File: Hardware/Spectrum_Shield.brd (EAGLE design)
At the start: 59.7 x 53.3 mm, 27 parts, among them U1 ARDUINO_R3_SHIELD, U2 MSGEQ7SOIC, U3 MSGEQ7SOIC

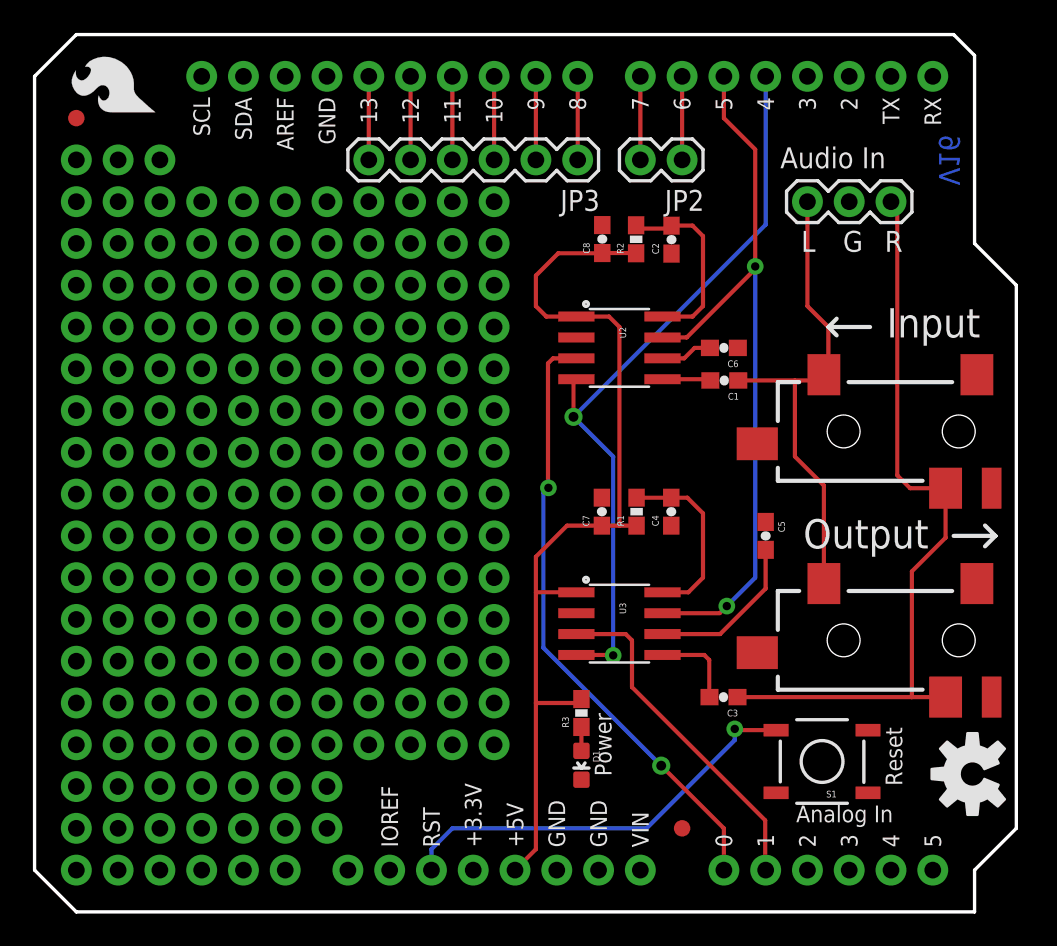
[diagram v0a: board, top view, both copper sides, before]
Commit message: Added stand offs, fixed silk.  QC list / attributes
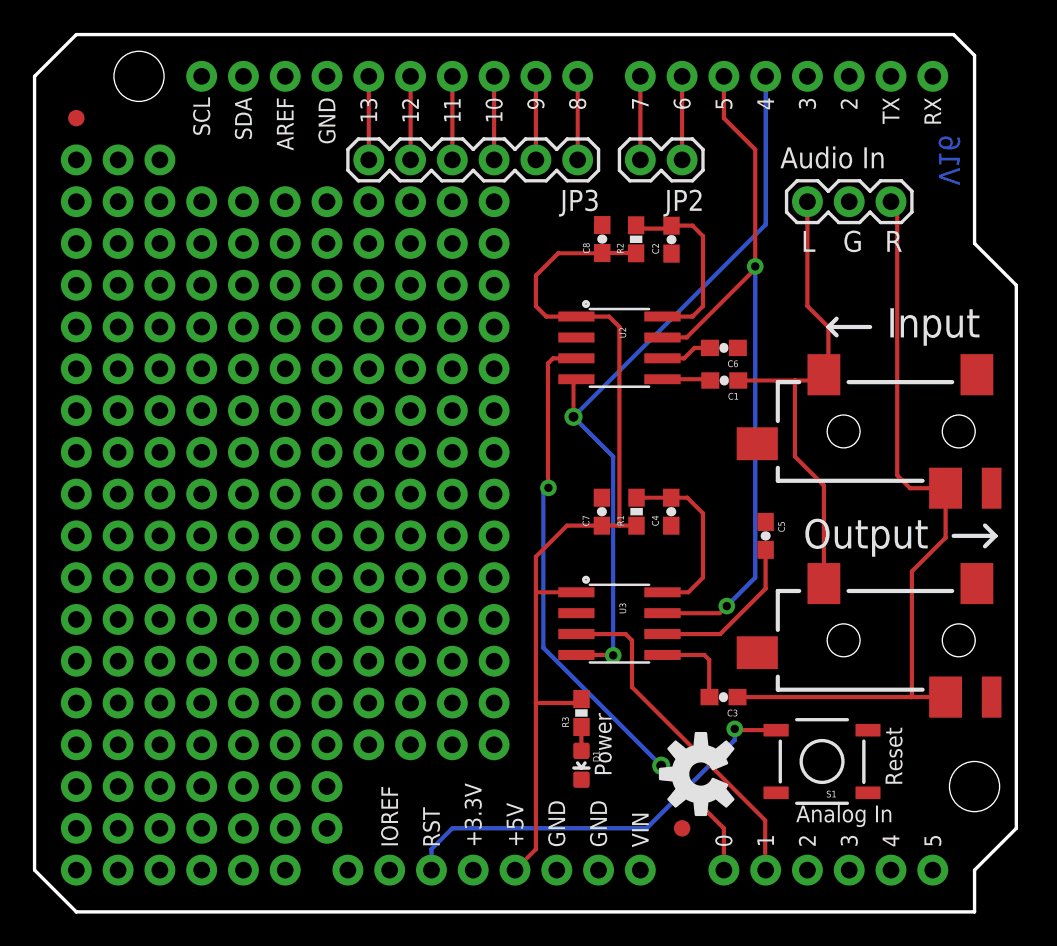
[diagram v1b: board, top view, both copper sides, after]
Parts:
- removed LOGO2: SFE_LOGO_FLAME.2_INCH, SparkFun-Aesthetics:SFE_LOGO_FLAME_.2
- added U$1, U$3: (no value), SparkFun-Electromechanical:STAND-OFF-TIGHT
- moved LOGO1 16.5 mm to (40.5, 8.38)
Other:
- board text added: "Chris Taylor"
- board text removed: "J. Lindblom"
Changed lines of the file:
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@@
 <?xml version="1.0" encoding="utf-8"?>
 <!DOCTYPE eagle SYSTEM "eagle.dtd">
-<eagle version="7.1.0">
+<eagle version="7.2.0">
 <drawing>
 <settings>
@@
 <wire x1="57.785" y1="23.495" x2="58.42" y2="22.86" width="0.254" layer="21"/>
 <wire x1="57.785" y1="22.225" x2="58.42" y2="22.86" width="0.254" layer="21"/>
-<text x="34.671" y="-15.367" size="1.778" layer="51" font="vector" ratio="12">J. Lindblom</text>
+<text x="39.751" y="-15.367" size="1.778" layer="51" font="vector" ratio="12">Chris Taylor</text>
 <text x="20.574" y="-17.907" size="1.778" layer="51" font="vector" ratio="12">Revised by: P. Alberts</text>
 <dimension x1="-20.32" y1="0" x2="-20.32" y2="53.34" x3="-19.05" y3="26.67" textsize="1.778" textratio="15" layer="47" unit="inch" visible="yes"/>
@@
 </element>
 <element name="FRAME1" library="SparkFun-Aesthetics" package="CREATIVE_COMMONS" value="FRAME-LETTER" x="8.89" y="-15.24"/>
-<element name="LOGO1" library="SparkFun-Aesthetics" package="OSHW-LOGO-M" value="OSHW-LOGOM" x="57.023" y="8.382" rot="R90"/>
-<element name="LOGO2" library="SparkFun-Aesthetics" package="SFE_LOGO_FLAME_.2" value="SFE_LOGO_FLAME.2_INCH" x="7.62" y="48.26" rot="R90"/>
+<element name="LOGO1" library="SparkFun-Aesthetics" package="OSHW-LOGO-M" value="OSHW-LOGOM" x="40.513" y="8.382" rot="R90"/>
 <element name="LOGO3" library="SparkFun-Aesthetics" package="SFE_LOGO_NAME_FLAME_.1" value="SFE_LOGO_NAME_FLAME.1_INCH" x="36.83" y="20.32" rot="MR90"/>
+<element name="U$1" library="SparkFun-Electromechanical" package="STAND-OFF-TIGHT" value="" x="57.15" y="7.62"/>
+<element name="U$3" library="SparkFun-Electromechanical" package="STAND-OFF-TIGHT" value="" x="6.35" y="50.8"/>
 </elements>
 <signals>

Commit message: Fixed QC Checklist Items
1) Currently there are two 4-way junctions: both below each MSGEQ7
symbol, each 4-way needs to split up into two 3-way junctions.

(2) On the R3 symbol the VCC net crosses over the RESET net. It would be
nice to reorganize these nets to eliminate the intersection all
together.

(3) The Audio jacks are currently named Audiojack1 and 2, these should
have a name that uses the proper connector prefix (JPx) x being a number

(4) Two vias have tStop and bStop polygons set over them: the first is
right next to the OSHW silk, and the other is below U2 (the upper MSGEQ7
IC). These are not used for testing

(5) Audio jacks need a name and value in BRD

(6) Need measures that include the standoffs

(7) As of now the name of the product is not on the board; the previous
rev was without a silk for the product name as well (figured I would
bring it up). Also, it would be nice to get an SFE flame on the top of
the board, like the previous rev.

that's it
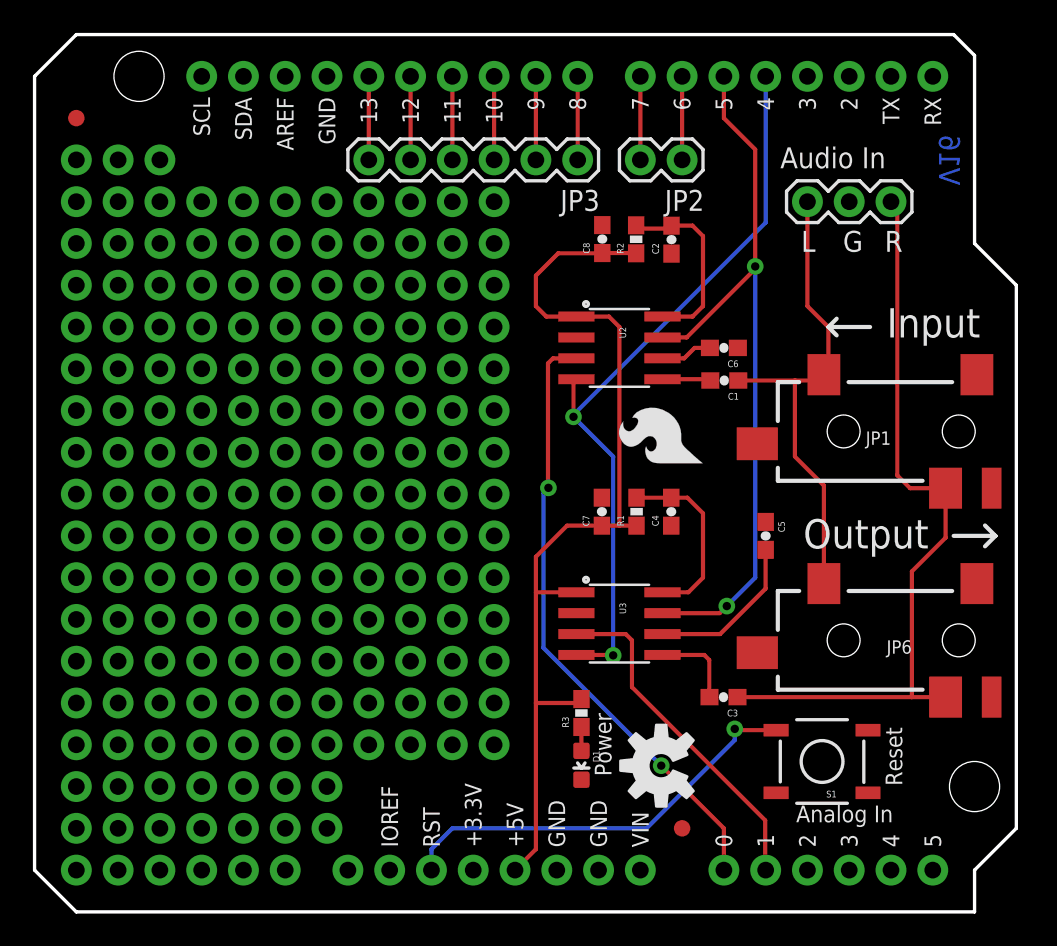
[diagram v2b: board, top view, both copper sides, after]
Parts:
- added LOGO2: SFE_LOGO_FLAME.2_INCH, SparkFun-Aesthetics:SFE_LOGO_FLAME_.2
- JP1, JP6: value (none) -> 3.5mm Audio Jack
- moved LOGO3 2.54 mm to (39.4, 20.3)
- moved LOGO1 2.47 mm to (38.1, 8.89)
- renumbered AUDIOJACK1 to JP1, AUDIOJACK2 to JP6
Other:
- board text added: "Center point to center point Stand Off distance"
- board text added: "Spectrum Shield"
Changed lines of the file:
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@@
 <?xml version="1.0" encoding="utf-8"?>
 <!DOCTYPE eagle SYSTEM "eagle.dtd">
-<eagle version="7.2.0">
+<eagle version="7.1.0">
 <drawing>
 <settings>
@@
 <layer number="47" name="Measures" color="7" fill="1" visible="no" active="yes"/>
 <layer number="48" name="Document" color="7" fill="1" visible="no" active="yes"/>
-<layer number="49" name="Reference" color="7" fill="1" visible="no" active="yes"/>
+<layer number="49" name="Reference" color="7" fill="1" visible="yes" active="yes"/>
 <layer number="50" name="dxf" color="7" fill="1" visible="no" active="yes"/>
 <layer number="51" name="tDocu" color="6" fill="1" visible="yes" active="yes"/>
@@
 <dimension x1="-20.32" y1="0" x2="-20.32" y2="53.34" x3="-19.05" y3="26.67" textsize="1.778" textratio="15" layer="47" unit="inch" visible="yes"/>
 <dimension x1="0" y1="59.69" x2="59.69" y2="59.69" x3="29.845" y3="58.42" textsize="1.778" textratio="15" layer="47" unit="inch" visible="yes"/>
+<dimension x1="6.35" y1="57.15" x2="57.15" y2="57.15" x3="31.75" y3="55.88" textsize="1.778" textratio="15" layer="47" unit="inch" visible="yes"/>
+<dimension x1="67.31" y1="7.62" x2="67.31" y2="50.8" x3="68.58" y3="29.21" textsize="1.778" textratio="15" layer="47" unit="inch" visible="yes"/>
+<text x="71.12" y="12.7" size="0.8128" layer="47" font="vector" ratio="15" rot="R90">Center point to center point Stand Off distance</text>
+<text x="46.99" y="55.88" size="0.8128" layer="47" font="vector" ratio="15" rot="R180">Center point to center point Stand Off distance</text>
+<text x="39.37" y="34.29" size="1.27" layer="22" font="vector" ratio="15" rot="MR270">Spectrum Shield</text>
 </plain>
 <attributes>
@@
 </autorouter>
 <elements>
-<element name="C1" library="SparkFun-Capacitors" package="0603-CAP" value="1nF" x="41.9354" y="32.3088" rot="R180">
+<element name="C1" library="SparkFun-Capacitors" package="0603-CAP" value="1nF" x="41.9354" y="32.3088" smashed="yes" rot="R180">
 <attribute name="PROD_ID" value="CAP-07886" x="41.9354" y="32.3088" size="1.778" layer="27" rot="R180" display="off"/>
 <attribute name="VALUE" value="1nF" x="41.9354" y="32.3088" size="1.778" layer="27" rot="R180" display="off"/>
+<attribute name="NAME" x="42.8244" y="31.5468" size="0.4064" layer="25" font="vector" rot="R180"/>
+<attribute name="VALUE" x="41.6814" y="31.5468" size="0.4064" layer="27" font="vector" rot="R180"/>
 </element>
 <element name="C2" library="SparkFun-Capacitors" package="0603-CAP" value="33pF" x="38.724840625" y="40.87368125" rot="R90">
@@
 <element name="JP4" library="SparkFun" package="FIDUCIAL-1X2" value="FIDUCIAL1X2" x="39.37" y="5.08"/>
 <element name="JP5" library="SparkFun" package="FIDUCIAL-1X2" value="FIDUCIAL1X2" x="2.54" y="48.26"/>
-<element name="AUDIOJACK1" library="SparkFun-Connectors" package="AUDIO-JACK-3.5MM-SMD" value="" x="59.69" y="29.21" rot="R180">
+<element name="JP1" library="SparkFun-Connectors" package="AUDIO-JACK-3.5MM-SMD" value="3.5mm Audio Jack" x="59.69" y="29.21" smashed="yes" rot="R180">
 <attribute name="PROD_ID" value="CONN-10353" x="59.69" y="29.21" size="1.778" layer="27" font="vector" ratio="15" rot="R180" display="off"/>
-</element>
-<element name="AUDIOJACK2" library="SparkFun-Connectors" package="AUDIO-JACK-3.5MM-SMD" value="" x="59.69" y="16.51" rot="R180">
+<attribute name="NAME" x="52.07" y="29.21" size="0.8128" layer="25" font="vector" rot="R180"/>
+<attribute name="VALUE" x="57.15" y="27.94" size="0.8128" layer="27" font="vector" rot="R180"/>
+</element>
+<element name="JP6" library="SparkFun-Connectors" package="AUDIO-JACK-3.5MM-SMD" value="3.5mm Audio Jack" x="59.69" y="16.51" smashed="yes" rot="R180">
 <attribute name="PROD_ID" value="CONN-10353" x="59.69" y="16.51" size="1.778" layer="27" font="vector" ratio="15" rot="R180" display="off"/>
+<attribute name="NAME" x="53.34" y="16.51" size="0.8128" layer="25" font="vector" rot="R180"/>
+<attribute name="VALUE" x="57.15" y="17.78" size="0.8128" layer="27" font="vector" rot="R180"/>
 </element>
 <element name="FRAME1" library="SparkFun-Aesthetics" package="CREATIVE_COMMONS" value="FRAME-LETTER" x="8.89" y="-15.24"/>
-<element name="LOGO1" library="SparkFun-Aesthetics" package="OSHW-LOGO-M" value="OSHW-LOGOM" x="40.513" y="8.382" rot="R90"/>
-<element name="LOGO3" library="SparkFun-Aesthetics" package="SFE_LOGO_NAME_FLAME_.1" value="SFE_LOGO_NAME_FLAME.1_INCH" x="36.83" y="20.32" rot="MR90"/>
+<element name="LOGO1" library="SparkFun-Aesthetics" package="OSHW-LOGO-M" value="OSHW-LOGOM" x="38.1" y="8.89" rot="R90"/>
+<element name="LOGO3" library="SparkFun-Aesthetics" package="SFE_LOGO_NAME_FLAME_.1" value="SFE_LOGO_NAME_FLAME.1_INCH" x="39.37" y="20.32" rot="MR90"/>
 <element name="U$1" library="SparkFun-Electromechanical" package="STAND-OFF-TIGHT" value="" x="57.15" y="7.62"/>
 <element name="U$3" library="SparkFun-Electromechanical" package="STAND-OFF-TIGHT" value="" x="6.35" y="50.8"/>
+<element name="LOGO2" library="SparkFun-Aesthetics" package="SFE_LOGO_FLAME_.2" value="SFE_LOGO_FLAME.2_INCH" x="40.894" y="26.924" rot="R90"/>
 </elements>
 <signals>
 <signal name="GND">
 <contactref element="C6" pad="1"/>
-<contactref element="C2" pad="1"/>
 <contactref element="C8" pad="2"/>
-<contactref element="C4" pad="1"/>
 <contactref element="C5" pad="1"/>
 <contactref element="C7" pad="2"/>
@@
 <vertex x="55.88" y="53.34"/>
 </polygon>
-<contactref element="AUDIOJACK2" pad="SLEEVE"/>
-<contactref element="AUDIOJACK1" pad="SLEEVE"/>
+<contactref element="JP6" pad="SLEEVE"/>
+<contactref element="JP1" pad="SLEEVE"/>
+<contactref element="C4" pad="1"/>
+<contactref element="C2" pad="1"/>
 </signal>
 <signal name="RESET">
@@
 <contactref element="U3" pad="4"/>
 <via x="35.179" y="15.5956" extent="1-16" drill="0.508"/>
-<via x="32.766" y="30.099" extent="1-16" drill="0.6"/>
-<wire x1="32.766" y1="30.099" x2="32.766" y2="32.2072" width="0.254" layer="1"/>
 <wire x1="32.766" y1="32.2072" x2="32.9438" y2="32.385" width="0.254" layer="1"/>
 <wire x1="32.766" y1="30.099" x2="35.179" y2="27.686" width="0.254" layer="16"/>
@@
 <wire x1="32.9438" y1="15.621" x2="35.1536" y2="15.621" width="0.254" layer="1"/>
 <wire x1="35.1536" y1="15.621" x2="35.179" y2="15.5956" width="0.254" layer="1"/>
-<wire x1="32.766" y1="30.099" x2="44.45" y2="41.783" width="0.254" layer="16"/>
-<wire x1="44.45" y1="41.783" x2="44.45" y2="50.8" width="0.254" layer="16"/>
+<wire x1="32.766" y1="32.2072" x2="32.766" y2="30.099" width="0.254" layer="1"/>
+<via x="32.766" y="30.099" extent="1-16" drill="0.508"/>
+<wire x1="32.766" y1="30.099" x2="32.766" y2="30.226" width="0.254" layer="16"/>
+<wire x1="32.766" y1="30.226" x2="44.45" y2="41.91" width="0.254" layer="16"/>
+<wire x1="44.45" y1="41.91" x2="44.45" y2="50.8" width="0.254" layer="16"/>
 </signal>
 <signal name="N$1">
@@
 <contactref element="U2" pad="3"/>
 <via x="31.242" y="25.781" extent="1-16" drill="0.508"/>
-<wire x1="30.9372" y1="16.0528" x2="38.1" y2="8.89" width="0.254" layer="16"/>
-<via x="38.1" y="8.89" extent="1-16" drill="0.6"/>
 <wire x1="32.9438" y1="33.655" x2="31.5214" y2="33.655" width="0.254" layer="1"/>
 <wire x1="31.5214" y1="33.655" x2="31.2166" y2="33.3502" width="0.254" layer="1"/>
@@
 <wire x1="30.9372" y1="16.0528" x2="30.9372" y2="25.4762" width="0.254" layer="16"/>
 <wire x1="30.9372" y1="25.4762" x2="31.242" y2="25.781" width="0.254" layer="16"/>
-<wire x1="38.1" y1="8.89" x2="41.91" y2="5.08" width="0.254" layer="1"/>
-<wire x1="41.91" y1="5.08" x2="41.91" y2="2.54" width="0.254" layer="1"/>
+<wire x1="41.91" y1="2.54" x2="41.91" y2="5.08" width="0.254" layer="1"/>
+<wire x1="41.91" y1="5.08" x2="38.1" y2="8.89" width="0.254" layer="1"/>
+<via x="38.1" y="8.89" extent="1-16" drill="0.508"/>
+<wire x1="38.1" y1="8.89" x2="30.9372" y2="16.0528" width="0.254" layer="16"/>
 </signal>
 <signal name="ANALOG1">
@@
 <contactref element="C3" pad="1"/>
 <contactref element="AUDIO_IN" pad="3"/>
-<contactref element="AUDIOJACK1" pad="RING"/>
-<contactref element="AUDIOJACK2" pad="RING"/>
+<contactref element="JP1" pad="RING"/>
+<contactref element="JP6" pad="RING"/>
 <wire x1="54.61" y1="12.7" x2="55.03" y2="12.7" width="0.254" layer="1"/>
 <wire x1="55.03" y1="12.7" x2="55.39" y2="13.06" width="0.254" layer="1"/>
@@
 <contactref element="C1" pad="1"/>
 <contactref element="AUDIO_IN" pad="1"/>
-<contactref element="AUDIOJACK1" pad="TIP"/>
-<contactref element="AUDIOJACK2" pad="TIP"/>
+<contactref element="JP1" pad="TIP"/>
+<contactref element="JP6" pad="TIP"/>
 <wire x1="46.99" y1="43.18" x2="46.99" y2="36.83" width="0.254" layer="1"/>
 <wire x1="46.99" y1="36.83" x2="48.26" y2="35.56" width="0.254" layer="1"/>
